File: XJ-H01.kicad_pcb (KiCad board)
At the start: 2 copper layers, 59 x 99 mm, 22 parts, among them J1 01x04, J13 AC, J2 SCT_013, J5 P_01x08, Q1 BT139-600, SW1 SW_DIP_x08, SW2 SW_DIP_x08, SW3 SW_DIP_x08, SW4 SW_DIP_x08, SW5 SW_DIP_x02, U1 MOC3011M

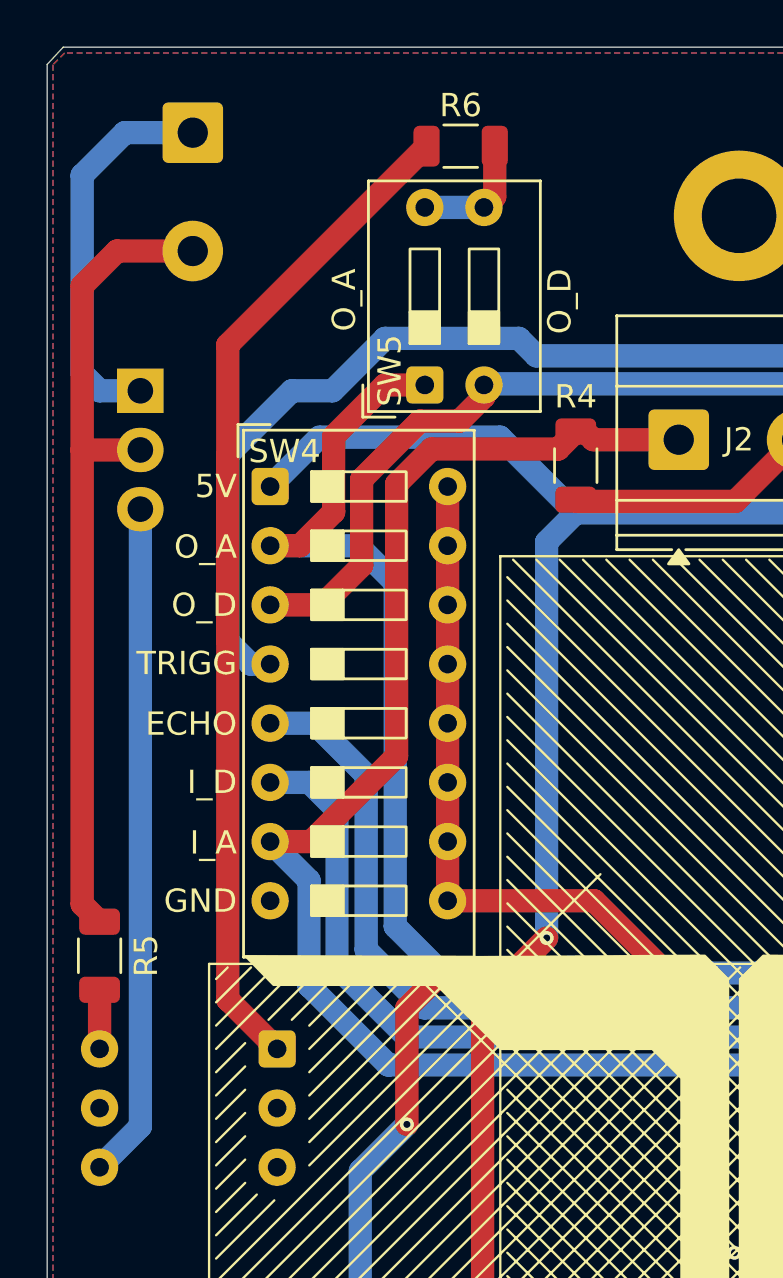
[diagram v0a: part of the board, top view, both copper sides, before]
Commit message: chore (XJ-H01): add change component position for tentative resize PCB
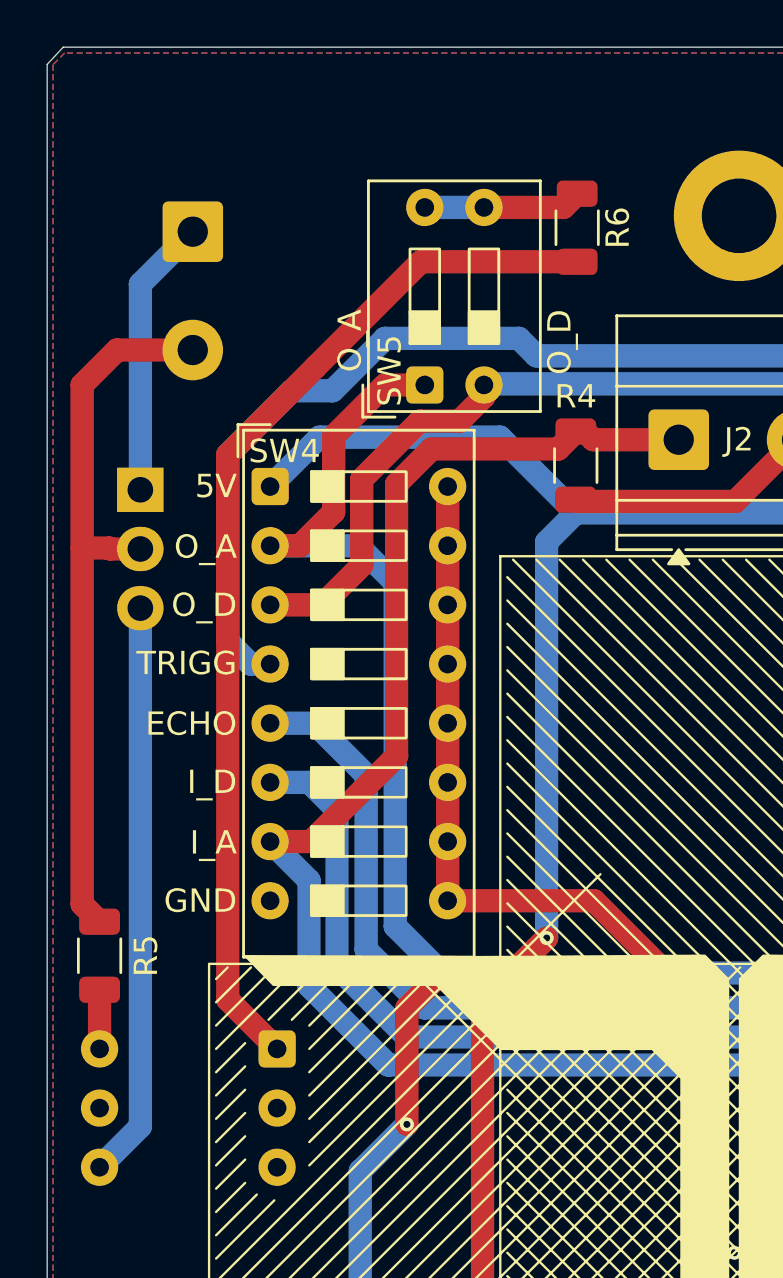
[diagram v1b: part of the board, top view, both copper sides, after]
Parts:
- moved R6 6.10 mm to (64.5, 50.0), turned to -90 degrees
- moved J13 4.25 mm to (48.0, 50.2)
- moved Q1 4.25 mm to (45.8, 61.2)
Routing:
- net AC_L: track 16.8 -> 12.0 mm
- net Net-(Q1-G): track 29.0 -> 24.7 mm
- net AC_SW: track 35.5 -> 31.2 mm
- net Net-(R6-Pad2): track 43.2 -> 44.8 mm
- net Net-(R6-Pad1): track 5.36 -> 6.79 mm
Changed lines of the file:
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@@
 	(footprint "Resistor_SMD:R_1206_3216Metric"
 		(layer "F.Cu")
-		(at 59.5 46.5 180)
+		(at 64.5 50 -90)
 		(descr "Resistor SMD 1206 (3216 Metric), square (rectangular) end terminal, IPC-7351 nominal, (Body size source: IPC-SM-782 page 72, https://www.pcb-3d.com/wordpress/wp-content/uploads/ipc-sm-782a_amendment_1_and_2.pdf), generated with kicad-footprint-generator")
 		(tags "resistor")
 		(property "Reference" "R6"
-			(at 0 1.75 0)
+			(at 0 -1.75 90)
 			(layer "F.SilkS")
 			(effects
@@
 		)
 		(property "Value" "330"
-			(at 0 1.83 0)
+			(at 3.75 0 90)
 			(layer "F.Fab")
 			(effects
@@
 		)
 		(property "Datasheet" "~"
-			(at 0 0 0)
+			(at 0 0 90)
 			(layer "F.Fab")
 			(hide yes)
@@
 		)
 		(property "Description" "Resistor, US symbol"
-			(at 0 0 0)
+			(at 0 0 90)
 			(layer "F.Fab")
 			(hide yes)
@@
 		)
 		(fp_text user "${REFERENCE}"
-			(at 0 0 0)
+			(at 0 0 90)
 			(layer "F.Fab")
 			(effects
@@
 		)
 		(pad "1" smd roundrect
-			(at -1.4625 0 180)
+			(at -1.4625 0 270)
 			(size 1.125 1.75)
 			(layers "F.Cu" "F.Mask" "F.Paste")
@@
 		)
 		(pad "2" smd roundrect
-			(at 1.4625 0 180)
+			(at 1.4625 0 270)
 			(size 1.125 1.75)
 			(layers "F.Cu" "F.Mask" "F.Paste")
@@
 	(footprint "Package_TO_SOT_THT:TO-220-3_Vertical"
 		(layer "B.Cu")
-		(at 45.75 57 -90)
+		(at 45.75 61.25 -90)
 		(descr "TO-220-3, Vertical, RM 2.54mm, see https://www.vishay.com/docs/66542/to-220-1.pdf, generated with kicad-footprint-generator TO_SOT_THT_generate.py")
 		(tags "TO-220-3 Vertical RM 2.54mm")
@@
 	(footprint "TerminalBlock_Phoenix:TerminalBlock_Phoenix_MKDS-1,5-2-5.08_1x02_P5.08mm_Horizontal"
 		(layer "B.Cu")
-		(at 48 45.92 -90)
+		(at 48 50.17 -90)
 		(descr "Terminal Block Phoenix MKDS-1,5-2-5.08, 2 pins, pitch 5.08mm, size 10.2x9.8mm, drill diameter 1.3mm, pad diameter 2.6mm, http://www.farnell.com/datasheets/100425.pdf, script-generated using https://gitlab.com/kicad/libraries/kicad-footprint-generator/-/tree/master/scripts/TerminalBlock_Phoenix")
 		(tags "THT Terminal Block Phoenix MKDS-1,5-2-5.08 pitch 5.08mm size 10.2x9.8mm drill 1.3mm pad 2.6mm")
@@
 	)
 	(gr_text "O_D"
-		(at 63.75 51.75 90)
+		(at 63.75 53.5 90)
 		(layer "F.SilkS")
 		(effects
@@
 	)
 	(gr_text "O_A"
-		(at 54.5 51.75 90)
+		(at 54.75 53.5 90)
 		(layer "F.SilkS")
 		(effects
@@
 	)
 	(segment
-		(start 43.25 59.54)
-		(end 45.75 59.54)
+		(start 45.75 63.79)
+		(end 44.46 63.79)
 		(width 1)
 		(layer "F.Cu")
@@
 	)
 	(segment
-		(start 43.25 52.5)
-		(end 43.25 59.54)
+		(start 44.42 63.75)
+		(end 43.25 63.75)
 		(width 1)
 		(layer "F.Cu")
@@
 	)
 	(segment
-		(start 48 51)
-		(end 44.75 51)
+		(start 44.75 55.25)
+		(end 43.25 56.75)
 		(width 1)
 		(layer "F.Cu")
@@
 	(segment
 		(start 43.25 79.0375)
-		(end 43.25 59.54)
+		(end 44 79.7875)
 		(width 1)
 		(layer "F.Cu")
@@
 	)
 	(segment
-		(start 44 79.7875)
+		(start 43.25 56.75)
 		(end 43.25 79.0375)
 		(width 1)
@@
 	)
 	(segment
-		(start 44.75 51)
-		(end 43.25 52.5)
+		(start 44.46 63.79)
+		(end 44.42 63.75)
 		(width 1)
 		(layer "F.Cu")
@@
 	)
 	(segment
-		(start 45.08 45.92)
-		(end 48 45.92)
-		(width 1)
-		(layer "B.Cu")
-		(net 16)
-	)
-	(segment
-		(start 43.25 56.25)
-		(end 43.25 47.75)
-		(width 1)
-		(layer "B.Cu")
-		(net 16)
-	)
-	(segment
-		(start 45.75 57)
-		(end 44 57)
+		(start 48 55.25)
+		(end 44.75 55.25)
 		(width 1)
-		(layer "B.Cu")
-		(net 16)
+		(layer "F.Cu")
+		(net 15)
 	)
 	(segment
-		(start 43.25 47.75)
-		(end 45.08 45.92)
+		(start 45.75 52.42)
+		(end 45.75 61.25)
 		(width 1)
 		(layer "B.Cu")
@@
 	)
 	(segment
-		(start 44 57)
-		(end 43.25 56.25)
+		(start 48 50.17)
+		(end 45.75 52.42)
 		(width 1)
 		(layer "B.Cu")
@@
 	(segment
 		(start 45.75 88.58)
-		(end 45.75 62.08)
+		(end 45.75 66.33)
 		(width 1)
 		(layer "B.Cu")
@@
 	)
 	(segment
-		(start 60.9625 48.6675)
-		(end 60.5 49.13)
+		(start 60.5 49.13)
+		(end 63.9075 49.13)
 		(width 1)
 		(layer "F.Cu")
@@
 	)
 	(segment
-		(start 60.9625 46.5)
-		(end 60.9625 48.6675)
+		(start 63.9075 49.13)
+		(end 64.5 48.5375)
 		(width 1)
 		(layer "F.Cu")
@@
 	)
 	(segment
-		(start 58.0375 46.5)
-		(end 49.5 55.0375)
+		(start 49.5 59.75)
+		(end 49.5 83.13)
 		(width 1)
 		(layer "F.Cu")
@@
 	)
 	(segment
-		(start 49.5 55.0375)
-		(end 49.5 83.13)
+		(start 64.5 51.4625)
+		(end 57.7875 51.4625)
+		(width 1)
+		(layer "F.Cu")
+		(net 20)
+	)
+	(segment
+		(start 57.7875 51.4625)
+		(end 53.25 56)
+		(width 1)
+		(layer "F.Cu")
+		(net 20)
+	)
+	(segment
+		(start 53.25 56)
+		(end 49.5 59.75)
 		(width 1)
 		(layer "F.Cu")
@@
 		(min_thickness 0.25)
 		(filled_areas_thickness no)
-		(fill yes
+		(fill
 			(thermal_gap 0.5)
 			(thermal_bridge_width 0.5)
